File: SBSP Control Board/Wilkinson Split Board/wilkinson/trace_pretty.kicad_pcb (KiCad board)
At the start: 4 copper layers, 46.5 x 134.2 mm, 45 parts, among them J1 Conn_01x02_Socket, J10 Conn_Coaxial, J11 Conn_Coaxial, J12 Conn_Coaxial, J2 Conn_01x02_Socket, J5 Conn_Coaxial, J6 Conn_Coaxial, J7 Conn_Coaxial, J8 Conn_Coaxial, J9 Conn_Coaxial, U1 ADAR1000ACCZN, U2 SN74AVC4T245PW, U3 ADAR1000ACCZN

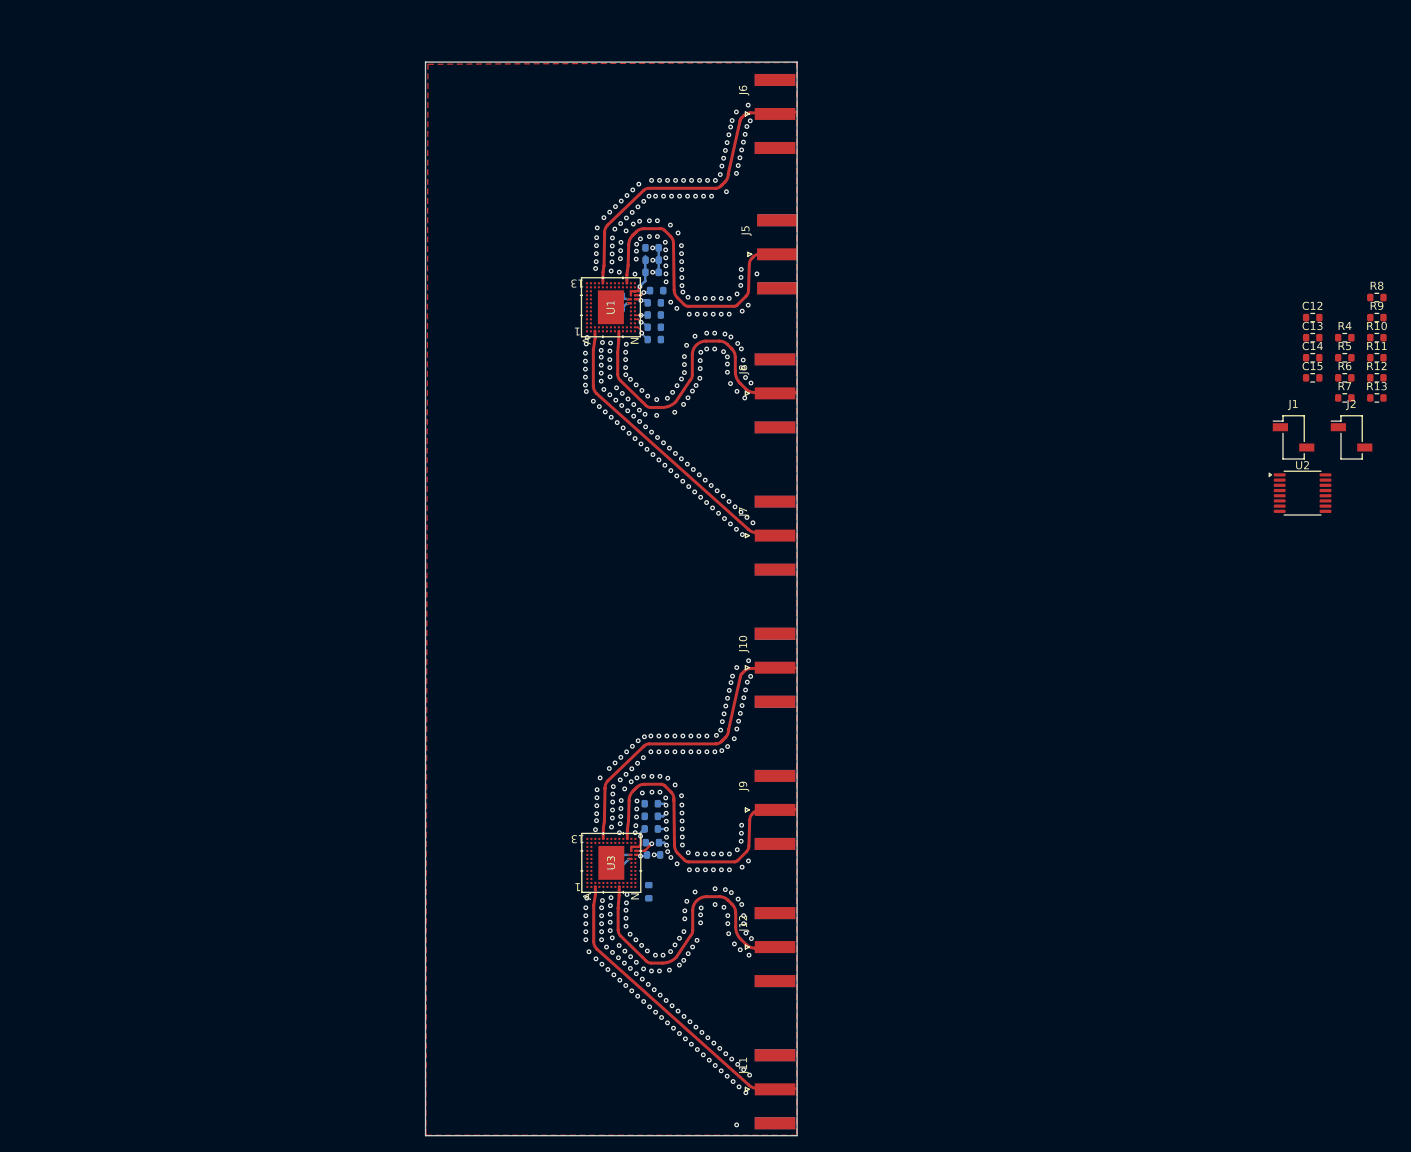
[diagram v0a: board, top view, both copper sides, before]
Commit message: fixed routing
monday: 5 hrs: talked to fayed about what exactly we needed to do, emailed fathy about what we do, get approval, re do schematic and layout to get wilkinson layout started. started workin on new schematic, started creating the adar1000 footprint and sch symbol, re did board outline and got traces from xmicrowave board, started doing layout for adar supporting passive components.

tuesday, 3 hrs (12-3), worked on adding level shifting circuit and began designing schematic for level shifting and ensuring each power level was correct and the schematic was equal in function to the evaluation board schematic.

wednesday: 5 (10-3), further schematic work, finished schematic, and then began layout for board. got wilkinson geometry from fayed and began its implementation into the design. layout is not done yet, but should not take much longer.

thursday: 5 (10-3)more layout work on the schematic, finished the level shifting circuit and added the power side to the layout and circuit.
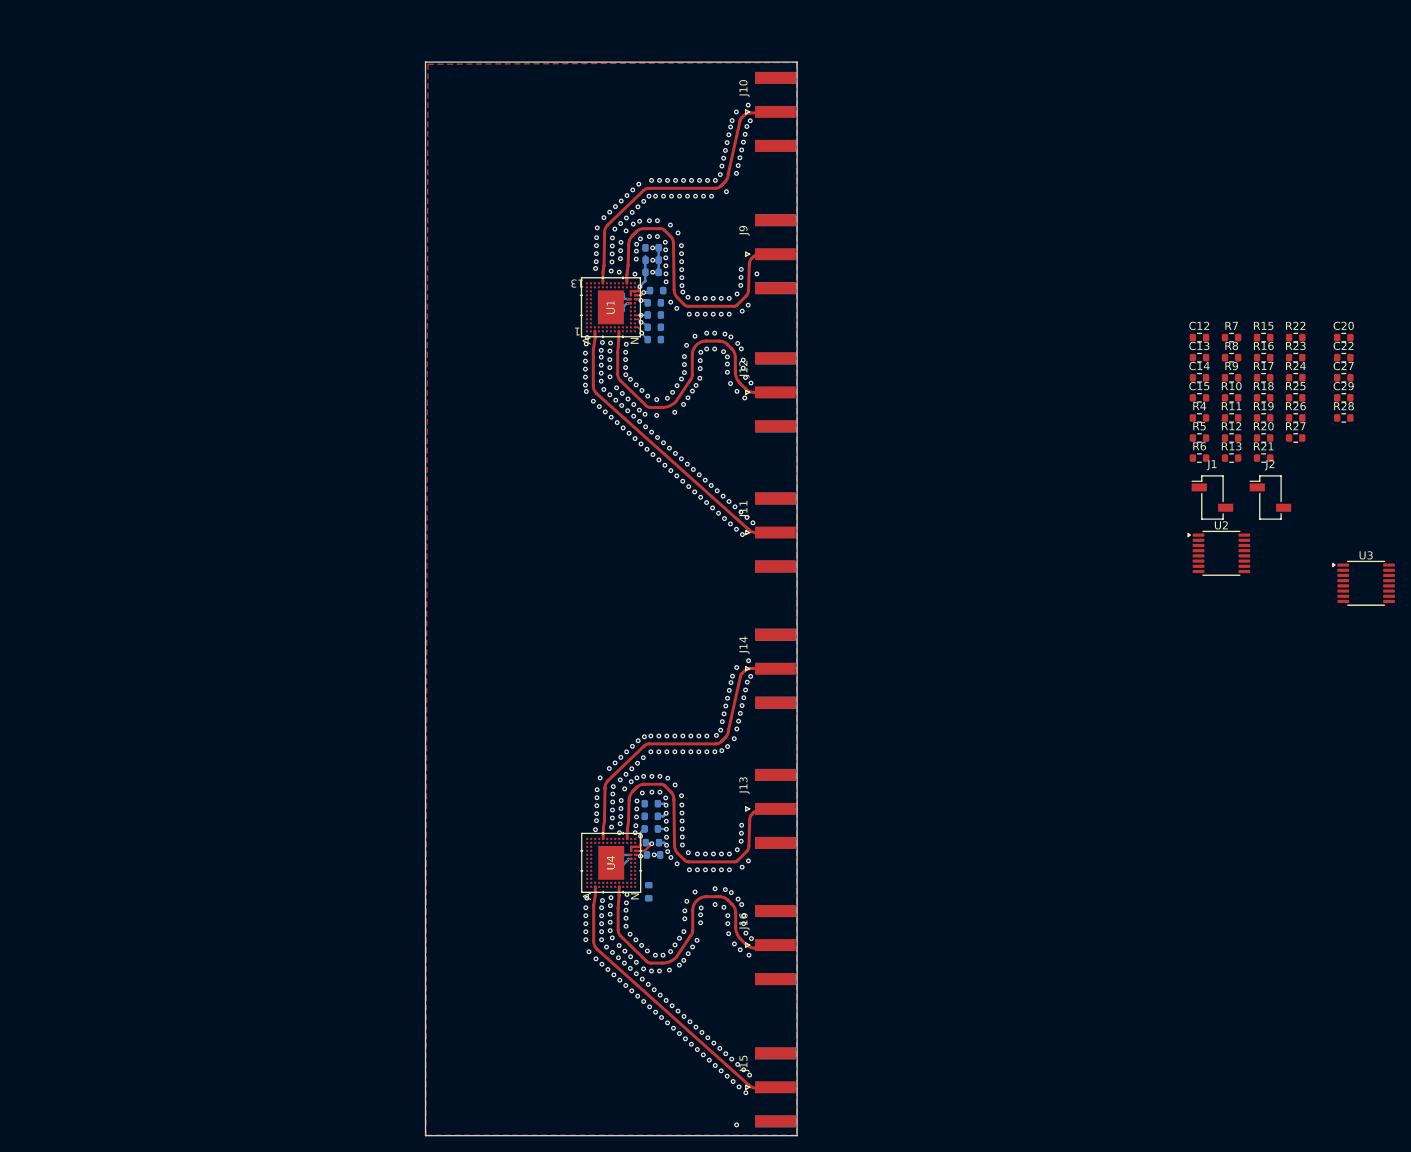
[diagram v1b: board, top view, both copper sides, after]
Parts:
- removed J5, J6, J7, J8: Conn_Coaxial, Connector_Coaxial:SMA_Amphenol_132289_EdgeMount
- added C20: 100pF, Resistor_SMD:R_0603_1608Metric, F.Cu at (531.2, 95.3)
- added C22: 4.7pF, Resistor_SMD:R_0603_1608Metric, F.Cu at (531.2, 97.8)
- added C27: 1uf, Resistor_SMD:R_0603_1608Metric, F.Cu at (531.2, 100.3)
- added C29: 1uf, Resistor_SMD:R_0603_1608Metric, F.Cu at (531.2, 102.8)
- added J13: Conn_Coaxial, Connector_Coaxial:SMA_Amphenol_132289_EdgeMount, F.Cu at (460.1, 154.2)
- added J14: Conn_Coaxial, Connector_Coaxial:SMA_Amphenol_132289_EdgeMount, F.Cu at (460.1, 136.7)
- added J15: Conn_Coaxial, Connector_Coaxial:SMA_Amphenol_132289_EdgeMount, F.Cu at (460.1, 189.0)
- added J16: Conn_Coaxial, Connector_Coaxial:SMA_Amphenol_132289_EdgeMount, F.Cu at (460.1, 171.2)
- added R15: 10k, Resistor_SMD:R_0603_1608Metric, F.Cu at (521.2, 95.3)
- added R16: 10k, Resistor_SMD:R_0603_1608Metric, F.Cu at (521.2, 97.8)
- added R17: 10k, Resistor_SMD:R_0603_1608Metric, F.Cu at (521.2, 100.3)
- added R18: 10k, Resistor_SMD:R_0603_1608Metric, F.Cu at (521.2, 102.8)
- added R19: 0, Resistor_SMD:R_0603_1608Metric, F.Cu at (521.2, 105.3)
- added R20: 10k, Resistor_SMD:R_0603_1608Metric, F.Cu at (521.2, 107.8)
- added R21: 0, Resistor_SMD:R_0603_1608Metric, F.Cu at (521.2, 110.3)
- added R22: 0, Resistor_SMD:R_0603_1608Metric, F.Cu at (525.2, 95.3)
- added R23: 10k, Resistor_SMD:R_0603_1608Metric, F.Cu at (525.2, 97.8)
- added R24: 10k, Resistor_SMD:R_0603_1608Metric, F.Cu at (525.2, 100.3)
- added R25: 10k, Resistor_SMD:R_0603_1608Metric, F.Cu at (525.2, 102.8)
- added R26: 0, Resistor_SMD:R_0603_1608Metric, F.Cu at (525.2, 105.3)
- added R27: 0, Resistor_SMD:R_0603_1608Metric, F.Cu at (525.2, 107.8)
- added R28: 10k, Resistor_SMD:R_0603_1608Metric, F.Cu at (531.2, 105.3)
- added U4: ADAR1000ACCZN, adar1000:CC-88-1_ADI, F.Cu at (439.6, 160.9)
- C16: value 100pF -> 10pF
- C17: value 0.01uF -> 0.1uF
- C18: value 4.7pF -> 10pF
- C19: value 1uf -> 0.1uF
- C21: value 1uf -> 0.01uF
- U3: value ADAR1000ACCZN -> SN74AVC4T245PW; footprint adar1000:CC-88-1_ADI -> Package_SO:TSSOP-16_4.4x5mm_P0.65mm
- moved U3 100.6 mm to (534.0, 126.0), turned to 0 degrees
- moved J11 69.6 mm to (460.1, 119.6)
- moved J10 69.5 mm to (460.1, 67.1)
- moved J9 69.5 mm to (460.1, 84.8)
- moved J12 69.3 mm to (460.1, 102.1)
- moved R4 20.8 mm to (513.1, 105.3)
- moved R5 20.8 mm to (513.1, 107.8)
- moved R6 20.8 mm to (513.1, 110.3)
- moved R11 19.7 mm to (517.2, 105.3)
- moved R8 19.7 mm to (517.2, 97.8)
- moved R10 19.7 mm to (517.2, 102.8)
- moved R12 19.7 mm to (517.2, 107.8)
- moved R13 19.7 mm to (517.2, 110.3)
- moved R9 19.7 mm to (517.2, 100.3)
- moved R7 16.0 mm to (517.2, 95.3)
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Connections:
- C16 pad 1: +3.3V -> GND
- C16 pad 2: GND -> +3V3
- C17 pad 1: +3.3V -> GND
- C17 pad 2: GND -> +3V3
- C18 pad 1: +3.3V -> +1.8V
- C19 pad 1: Net-(U3B-CREG1) -> +1.8V
- C21 pad 1: Net-(U3B-CREG2) -> +3.3V
- C23 pad 1: Net-(U3B-CREG3) -> Net-(U4B-CREG1)
- C25 pad 1: Net-(U3B-CREG4) -> Net-(U4B-CREG2)
- J10 pad 1: OUT6 -> OUT2
- J11 pad 1: OUT7 -> OUT3
- J12 pad 1: OUT8 -> OUT4
- J9 pad 1: OUT5 -> OUT1
- R14 pad 2: Net-(U3A-RX_LOAD) -> /GPIO5
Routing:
- net +1.8V: track 0.00 -> 5.81 mm, vias 0 -> 2
- net Net-(U4B-CREG1): track 0.00 -> 3.23 mm, vias 0 -> 1
- net Net-(U3B-CREG3): track 3.23 -> 0.00 mm, vias 1 -> 0
- net +3.3V: track 10.1 -> 7.49 mm
- net +3V3: track 0.00 -> 2.31 mm, vias 0 -> 2
- net GND: track 10.6 -> 8.26 mm, vias 484 -> 481
- net Net-(U3B-CREG1): track 1.81 -> 0.00 mm, vias 1 -> 0
- net Net-(U4B-CREG2): track 0.00 -> 1.58 mm, vias 0 -> 1
- net Net-(U3B-CREG4): track 1.58 -> 0.00 mm, vias 1 -> 0
- net Net-(U3B-CREG2): track 1.33 -> 0.00 mm, vias 1 -> 0
- net OUT8: vias 0 -> 1

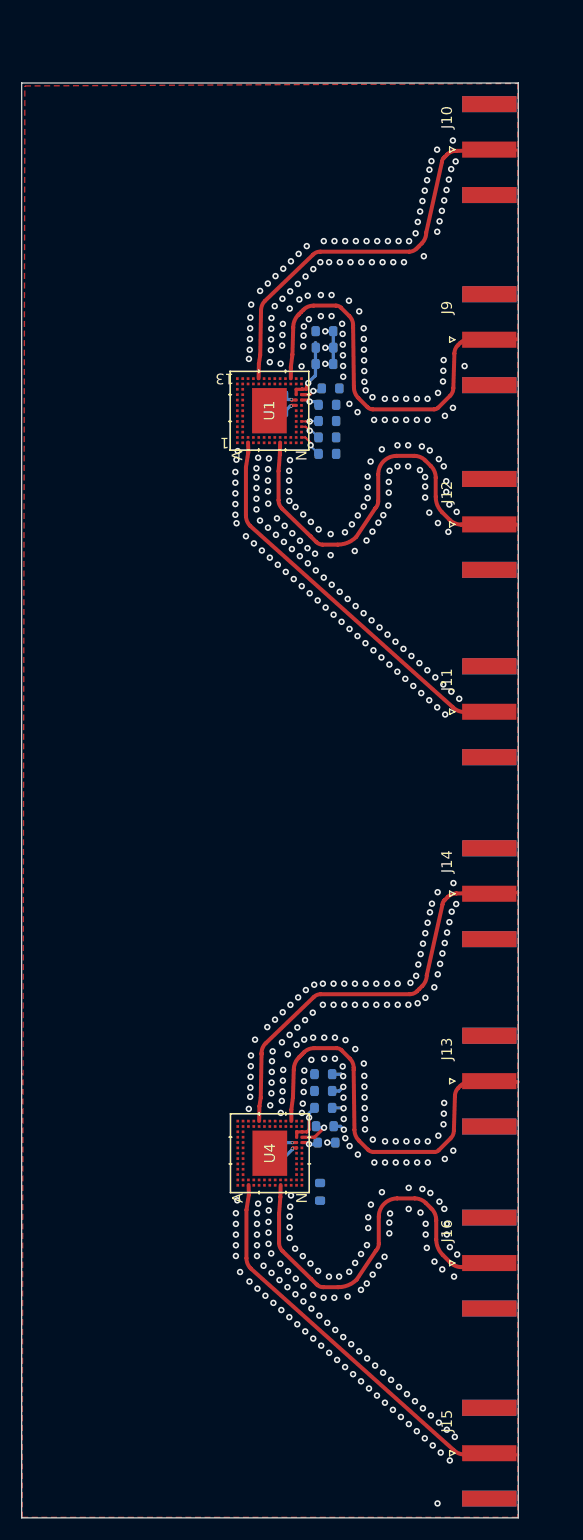
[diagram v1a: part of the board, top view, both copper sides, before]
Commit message: added wilkinson geometry
11:00 to 3:00

learned from nolan how the thing works and how to run and use it/test it. I then worked on the control circuit testing and wrote report on it. individually tested every patch to ensure the values matched the MATLAB sims. this took about 2 hours. the next two hours was spent working on the 1-8 splitter board. I finished adding the wilkinson geometry onto the board and began laying out the passive components.
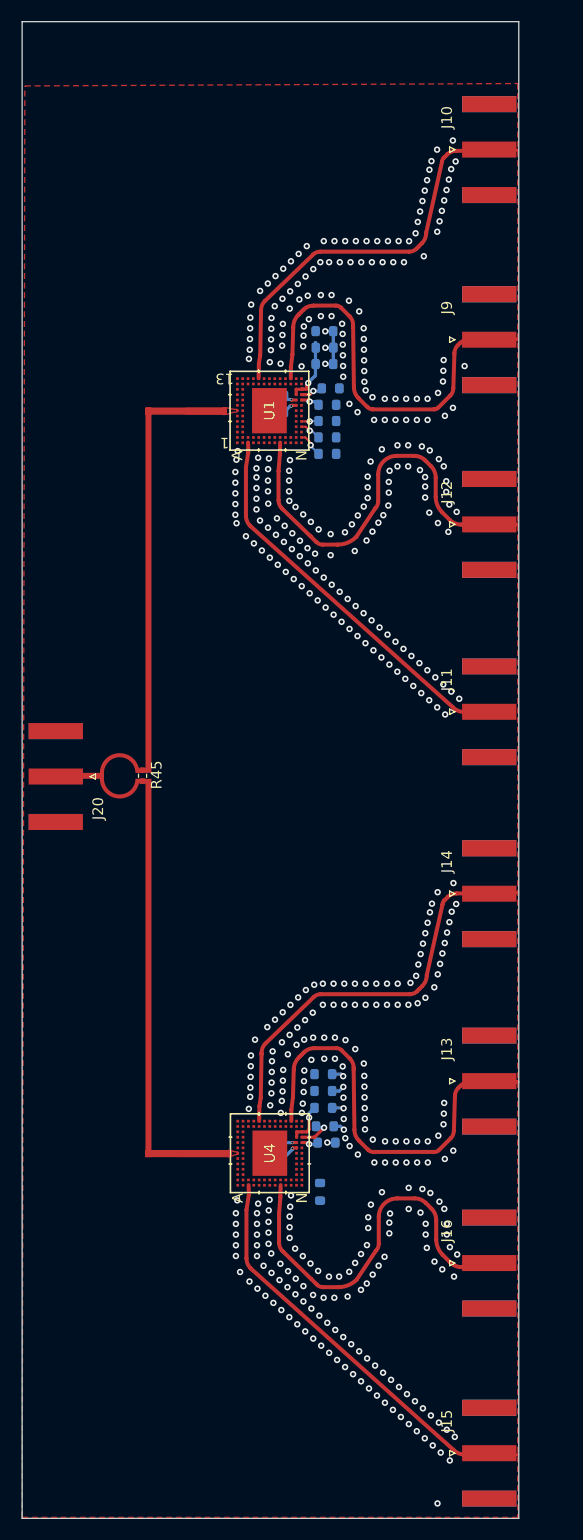
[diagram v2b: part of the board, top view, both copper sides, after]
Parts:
- added J20: Conn_Coaxial, Connector_Coaxial:SMA_Amphenol_132289_EdgeMount, F.Cu at (419.6, 125.7)
- added R45: 100, Resistor_SMD:R_0402_1005Metric, F.Cu at (427.7, 125.6)
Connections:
- U1 pad A7: /PLL_IN -> PLL_IN
- U4 pad A7: /TX1/PLL_IN -> PLL_IN
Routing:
- net PLL_IN: track 0.00 -> 8.26 mm
- added copper zone on F.Cu, net PLL_IN
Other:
- board size 46.5 x 134.2 mm -> 46.4 x 140 mm
